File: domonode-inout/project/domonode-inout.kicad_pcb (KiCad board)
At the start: 2 copper layers, 95 x 80 mm, 54 parts, among them P1 CONN_01X03, P10 CONN_01X02, P11 CONN_01X02, P12 CONN_01X02, P13 CONN_01X02, P2 CONN_2x5, P3 CONN_01X03, P4 CONN_01X03, P5 CONN_01X03, P6 CONN_01X02, P7 CONN_01X02, P8 CONN_01X02, P9 CONN_01X02, U1 HLK-PM01, U2 PCA9555, U3 TLP620, U4 TLP620, U5 TLP620, U6 24LC02

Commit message: Updated DomoNode-Inout to 1.1.2 (improved connectors footprints)
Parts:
- added P2: Conn_01x04, AAA mie lib verificate:KF2EDGK-5.08-4, F.Cu at (123.6, 126.4)
- P1, P3, P4, P5: value CONN_01X03 -> CONN_01X02; footprint AAA mie lib verificate:AK300-3 -> AAA mie lib verificate:KF2EDGK-5.08-2
- U3, U4, U5: footprint AAA mie lib verificate:DIP-4_W7.62mm_e_SOT-4 -> Housings_DIP:DIP-4_W7.62mm
- moved P3 15.1 mm to (143.9, 126.4)
- moved P4 10.1 mm to (154.1, 126.4)
- moved P5 4.99 mm to (164.2, 126.4)
- moved P1 0.65 mm to (113.4, 126.4)
- renumbered P2 to J1
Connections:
- P3 pad 1: /RL2P -> /I1L
- P3 pad 2: /RL3P -> /I1N
- P4 pad 1: /I1L -> /I2L
- P4 pad 2: /I1N -> /I2N
- P5 pad 1: /I2N -> /I3L
- P5 pad 2: /I3L -> /I3N
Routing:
- net /I2L: track 12.5 -> 14.4 mm
- net /I2N: track 13.4 -> 15.2 mm
- net /I1N: track 12.9 -> 14.6 mm
- net Net-(R11-Pad1): track 9.80 -> 8.22 mm
- net /I3L: track 18.9 -> 20.4 mm
- net /I3N: track 16.6 -> 15.8 mm
- net /L: track 58.3 -> 57.6 mm
- net /RL2P: track 15.2 -> 14.5 mm
- net /RL3P: track 13.1 -> 12.5 mm
- net /RL4P: track 14.4 -> 13.7 mm
- net /RL1P: track 16.8 -> 16.2 mm
- net /I1L: track 11.9 -> 11.3 mm
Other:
- board text added: "DomoNode-inout 1.1.2 Design by ndk@CSSHL.org"
- board text removed: "DomoNode-inout 1.1.1 Design by ndk@CSSHL.org"

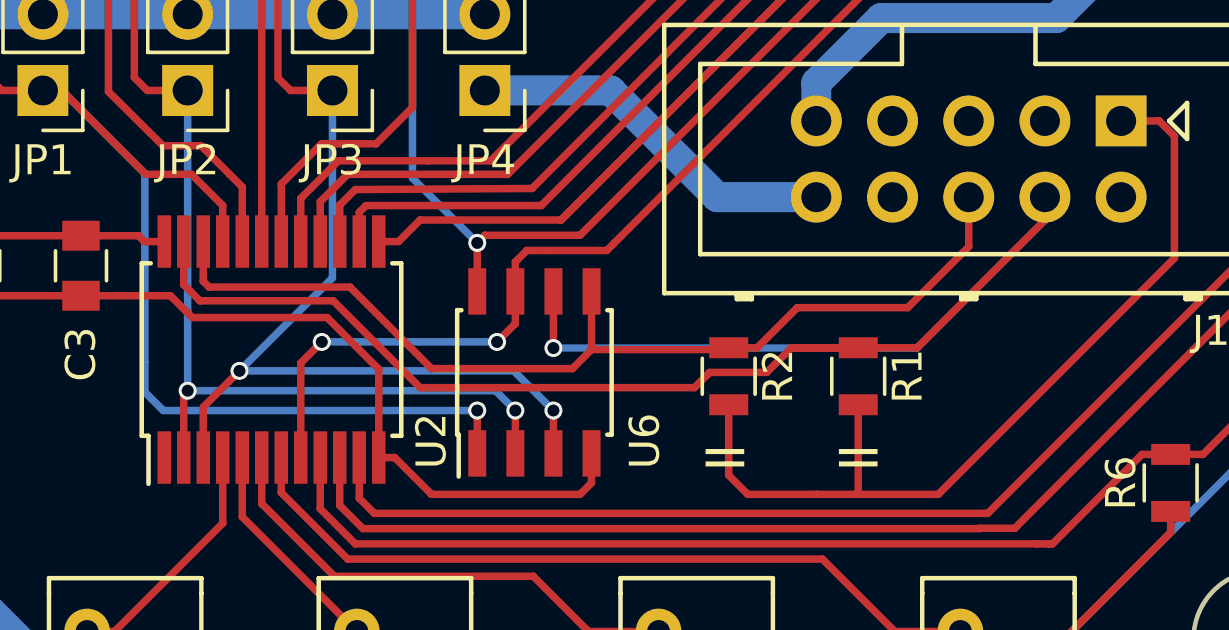
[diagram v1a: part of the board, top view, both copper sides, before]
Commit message: DomoNode-Inout: Fixed a really stupid error (swapped SCA/SCL on PCA9555); changed connector layout in schematic (from 1x10 to 2x5) for better readability
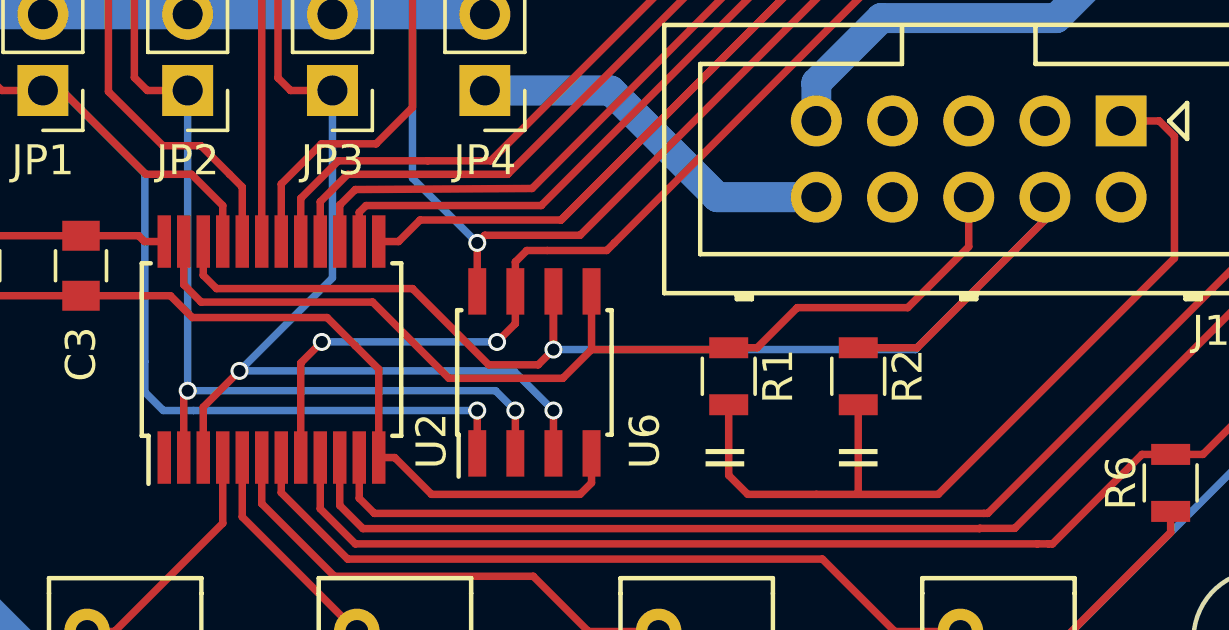
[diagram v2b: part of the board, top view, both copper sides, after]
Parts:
- moved R1 4.32 mm to (135.1, 85.5)
- moved R2 4.32 mm to (139.4, 85.5)
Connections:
- R1 pad 2: /SCL -> /SDA
- R2 pad 2: /SDA -> /SCL
- U2 pad 22: /SDA -> /SCL
- U2 pad 23: /SCL -> /SDA
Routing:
- net /SCL: track 56.9 -> 45.0 mm
- net /SDA: track 33.4 -> 34.4 mm
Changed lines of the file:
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@@
   (general
     (links 112)
-    (no_connects 1)
+    (no_connects 0)
     (area 70.765999 50.827 190.024572 139.608001)
     (thickness 1.6)
     (drawings 28)
-    (tracks 442)
+    (tracks 439)
     (zones 0)
     (modules 55)
@@
   (title_block
     (title DomoNode-InOut)
-    (date 2018-05-13)
-    (rev 1.1.2)
+    (date 2018-06-28)
+    (rev 1.1.3)
     (company CSSHL.org)
   )
@@
       (drillshape 0)
       (scaleselection 1)
-      (outputdirectory ../../../../../tmp/Domonode-inout-1.1.2/))
+      (outputdirectory ../../../../../tmp/Domonode-inout-1.1.3/))
   )
   (net 0 "")
@@
   )
   (module Resistors_SMD:R_0805 (layer F.Cu)
+    (at 135.128 85.471 90)
+    (descr "Resistor SMD 0805, reflow soldering, Vishay (see dcrcw.pdf)")
+    (tags "resistor 0805")
+    (attr smd)
+    (fp_text reference R1 (at 0 1.651 90) (layer F.SilkS)
+      (effects (font (size 1 1) (thickness 0.15)))
+    )
+    (fp_text value 10k (at 0 1.75 90) (layer F.Fab) hide
+      (effects (font (size 1 1) (thickness 0.15)))
+    )
+    (fp_text user %R (at 0 0 90) (layer F.Fab)
+      (effects (font (size 0.5 0.5) (thickness 0.075)))
+    )
+    (fp_line (start -1 0.62) (end -1 -0.62) (layer F.Fab) (width 0.1))
+    (fp_line (start 1 0.62) (end -1 0.62) (layer F.Fab) (width 0.1))
+    (fp_line (start 1 -0.62) (end 1 0.62) (layer F.Fab) (width 0.1))
+    (fp_line (start -1 -0.62) (end 1 -0.62) (layer F.Fab) (width 0.1))
+    (fp_line (start 0.6 0.88) (end -0.6 0.88) (layer F.SilkS) (width 0.12))
+    (fp_line (start -0.6 -0.88) (end 0.6 -0.88) (layer F.SilkS) (width 0.12))
+    (fp_line (start -1.55 -0.9) (end 1.55 -0.9) (layer F.CrtYd) (width 0.05))
+    (fp_line (start -1.55 -0.9) (end -1.55 0.9) (layer F.CrtYd) (width 0.05))
+    (fp_line (start 1.55 0.9) (end 1.55 -0.9) (layer F.CrtYd) (width 0.05))
+    (fp_line (start 1.55 0.9) (end -1.55 0.9) (layer F.CrtYd) (width 0.05))
+    (pad 1 smd rect (at -0.95 0 90) (size 0.7 1.3) (layers F.Cu F.Paste F.Mask)
+      (net 3 +3V3))
+    (pad 2 smd rect (at 0.95 0 90) (size 0.7 1.3) (layers F.Cu F.Paste F.Mask)
+      (net 4 /SDA))
+    (model ${KISYS3DMOD}/Resistors_SMD.3dshapes/R_0805.wrl
+      (at (xyz 0 0 0))
+      (scale (xyz 1 1 1))
+      (rotate (xyz 0 0 0))
+    )
+  )
+  (module Resistors_SMD:R_0805 (layer F.Cu)
     (at 139.446 85.471 90)
     (descr "Resistor SMD 0805, reflow soldering, Vishay (see dcrcw.pdf)")
     (tags "resistor 0805")
     (attr smd)
-    (fp_text reference R1 (at 0 1.651 90) (layer F.SilkS)
+    (fp_text reference R2 (at 0 1.651 90) (layer F.SilkS)
       (effects (font (size 1 1) (thickness 0.15)))
     )
@@
     (pad 2 smd rect (at 0.95 0 90) (size 0.7 1.3) (layers F.Cu F.Paste F.Mask)
       (net 5 /SCL))
-    (model ${KISYS3DMOD}/Resistors_SMD.3dshapes/R_0805.wrl
-      (at (xyz 0 0 0))
-      (scale (xyz 1 1 1))
-      (rotate (xyz 0 0 0))
-    )
-  )
-  (module Resistors_SMD:R_0805 (layer F.Cu)
-    (at 135.128 85.471 90)
-    (descr "Resistor SMD 0805, reflow soldering, Vishay (see dcrcw.pdf)")
-    (tags "resistor 0805")
-    (attr smd)
-    (fp_text reference R2 (at 0 1.651 90) (layer F.SilkS)
-      (effects (font (size 1 1) (thickness 0.15)))
-    )
-    (fp_text value 10k (at 0 1.75 90) (layer F.Fab) hide
-      (effects (font (size 1 1) (thickness 0.15)))
-    )
-    (fp_text user %R (at 0 0 90) (layer F.Fab)
-      (effects (font (size 0.5 0.5) (thickness 0.075)))
-    )
-    (fp_line (start -1 0.62) (end -1 -0.62) (layer F.Fab) (width 0.1))
-    (fp_line (start 1 0.62) (end -1 0.62) (layer F.Fab) (width 0.1))
-    (fp_line (start 1 -0.62) (end 1 0.62) (layer F.Fab) (width 0.1))
-    (fp_line (start -1 -0.62) (end 1 -0.62) (layer F.Fab) (width 0.1))
-    (fp_line (start 0.6 0.88) (end -0.6 0.88) (layer F.SilkS) (width 0.12))
-    (fp_line (start -0.6 -0.88) (end 0.6 -0.88) (layer F.SilkS) (width 0.12))
-    (fp_line (start -1.55 -0.9) (end 1.55 -0.9) (layer F.CrtYd) (width 0.05))
-    (fp_line (start -1.55 -0.9) (end -1.55 0.9) (layer F.CrtYd) (width 0.05))
-    (fp_line (start 1.55 0.9) (end 1.55 -0.9) (layer F.CrtYd) (width 0.05))
-    (fp_line (start 1.55 0.9) (end -1.55 0.9) (layer F.CrtYd) (width 0.05))
-    (pad 1 smd rect (at -0.95 0 90) (size 0.7 1.3) (layers F.Cu F.Paste F.Mask)
-      (net 3 +3V3))
-    (pad 2 smd rect (at 0.95 0 90) (size 0.7 1.3) (layers F.Cu F.Paste F.Mask)
-      (net 4 /SDA))
     (model ${KISYS3DMOD}/Resistors_SMD.3dshapes/R_0805.wrl
       (at (xyz 0 0 0))
@@
       (net 41 /A0))
     (pad 22 smd rect (at 3.6 -2.275 90) (size 1.75 0.45) (layers F.Cu F.Paste F.Mask)
+      (net 5 /SCL))
+    (pad 23 smd rect (at 3.6 -2.925 90) (size 1.75 0.45) (layers F.Cu F.Paste F.Mask)
       (net 4 /SDA))
-    (pad 23 smd rect (at 3.6 -2.925 90) (size 1.75 0.45) (layers F.Cu F.Paste F.Mask)
-      (net 5 /SCL))
     (pad 24 smd rect (at 3.6 -3.575 90) (size 1.75 0.45) (layers F.Cu F.Paste F.Mask)
       (net 1 +5V))
@@
   (segment (start 135.763 89.408) (end 138.049 89.408) (width 0.25) (layer F.Cu) (net 3))
   (segment (start 135.128 88.773) (end 135.763 89.408) (width 0.25) (layer F.Cu) (net 3))
+  (segment (start 117.54401 83.00001) (end 116.963 82.419) (width 0.25) (layer F.Cu) (net 4))
+  (segment (start 116.963 82.419) (end 116.963 80.982) (width 0.25) (layer F.Cu) (net 4))
+  (segment (start 130.556 84.582) (end 129.597991 85.540009) (width 0.25) (layer F.Cu) (net 4))
+  (segment (start 129.597991 85.540009) (end 125.800419 85.540009) (width 0.25) (layer F.Cu) (net 4))
+  (segment (start 125.800419 85.540009) (end 123.26042 83.00001) (width 0.25) (layer F.Cu) (net 4))
+  (segment (start 123.26042 83.00001) (end 117.54401 83.00001) (width 0.25) (layer F.Cu) (net 4))
   (segment (start 143.129 79.502) (end 143.129 81.153) (width 0.25) (layer F.Cu) (net 4) (status 10))
   (segment (start 141.097 83.185) (end 137.414 83.185) (width 0.25) (layer F.Cu) (net 4))
   (segment (start 143.129 81.153) (end 141.097 83.185) (width 0.25) (layer F.Cu) (net 4))
-  (segment (start 129.921 85.217) (end 125.222 85.217) (width 0.25) (layer F.Cu) (net 4))
-  (segment (start 117.613 80.982) (end 117.613 82.307) (width 0.25) (layer F.Cu) (net 4) (status 10))
-  (segment (start 125.222 85.217) (end 122.5042 82.4992) (width 0.25) (layer F.Cu) (net 4))
-  (segment (start 122.5042 82.4992) (end 117.8052 82.4992) (width 0.25) (layer F.Cu) (net 4))
-  (segment (start 117.8052 82.4992) (end 117.613 82.307) (width 0.25) (layer F.Cu) (net 4))
-  (segment (start 129.921 85.217) (end 130.556 84.582) (width 0.25) (layer F.Cu) (net 4))
-  (segment (start 135.128 84.521) (end 136.078 84.521) (width 0.25) (layer F.Cu) (net 4) (status 10))
   (segment (start 136.078 84.521) (end 137.414 83.185) (width 0.25) (layer F.Cu) (net 4))
   (segment (start 130.556 82.517) (end 130.556 84.582) (width 0.25) (layer F.Cu) (net 4) (status 10))
+  (segment (start 135.128 84.521) (end 136.078 84.521) (width 0.25) (layer F.Cu) (net 4) (status 10))
   (segment (start 135.1023 84.582) (end 130.556 84.582) (width 0.25) (layer F.Cu) (net 4) (status 10))
-  (segment (start 145.669 79.502) (end 145.669 80.264) (width 0.25) (layer B.Cu) (net 5) (status 30))
-  (via (at 129.286 84.5312) (size 0.6) (drill 0.4) (layers F.Cu B.Cu) (net 5))
-  (segment (start 129.286 84.5312) (end 141.4018 84.5312) (width 0.25) (layer B.Cu) (net 5))
-  (segment (start 141.4018 84.5312) (end 145.669 80.264) (width 0.25) (layer B.Cu) (net 5) (status 20))
+  (segment (start 129.286 84.582) (end 128.778 85.09) (width 0.25) (layer F.Cu) (net 5))
+  (segment (start 124.587 82.55) (end 127.127 85.09) (width 0.25) (layer F.Cu) (net 5))
+  (segment (start 118.056 82.55) (end 124.587 82.55) (width 0.25) (layer F.Cu) (net 5))
+  (segment (start 117.613 82.107) (end 117.613 80.982) (width 0.25) (layer F.Cu) (net 5))
+  (segment (start 117.613 82.107) (end 118.056 82.55) (width 0.25) (layer F.Cu) (net 5))
+  (segment (start 128.778 85.09) (end 127.127 85.09) (width 0.25) (layer F.Cu) (net 5))
+  (segment (start 145.669 79.502) (end 145.669 80.264) (width 0.25) (layer B.Cu) (net 5))
+  (segment (start 145.669 80.264) (end 141.351 84.582) (width 0.25) (layer B.Cu) (net 5))
+  (segment (start 129.286 84.582) (end 129.286 82.644) (width 0.25) (layer F.Cu) (net 5))
+  (via (at 129.286 84.582) (size 0.6) (drill 0.4) (layers F.Cu B.Cu) (net 5))
+  (segment (start 141.351 84.582) (end 129.286 84.582) (width 0.25) (layer B.Cu) (net 5))
+  (segment (start 141.412 84.521) (end 139.446 84.521) (width 0.25) (layer F.Cu) (net 5) (status 20))
   (segment (start 129.286 82.644) (end 129.286 84.5312) (width 0.25) (layer F.Cu) (net 5) (status 10))
   (segment (start 145.669 80.264) (end 141.412 84.521) (width 0.25) (layer F.Cu) (net 5) (status 10))
-  (segment (start 121.9454 82.9564) (end 124.841 85.852) (width 0.25) (layer F.Cu) (net 5))
-  (segment (start 136.398 85.344) (end 137.221 84.521) (width 0.25) (layer F.Cu) (net 5))
-  (segment (start 134.493 85.344) (end 136.398 85.344) (width 0.25) (layer F.Cu) (net 5))
-  (segment (start 133.985 85.852) (end 134.493 85.344) (width 0.25) (layer F.Cu) (net 5))
-  (segment (start 124.841 85.852) (end 133.985 85.852) (width 0.25) (layer F.Cu) (net 5))
-  (segment (start 137.221 84.521) (end 139.446 84.521) (width 0.25) (layer F.Cu) (net 5) (status 20))
-  (segment (start 116.963 80.982) (end 116.963 82.419) (width 0.25) (layer F.Cu) (net 5) (status 10))
-  (segment (start 117.5004 82.9564) (end 121.9454 82.9564) (width 0.25) (layer F.Cu) (net 5))
-  (segment (start 116.963 82.419) (end 117.5004 82.9564) (width 0.25) (layer F.Cu) (net 5))
-  (segment (start 139.446 84.521) (end 137.221 84.521) (width 0.25) (layer F.Cu) (net 5) (status 10))
-  (segment (start 141.412 84.521) (end 139.446 84.521) (width 0.25) (layer F.Cu) (net 5) (status 20))
   (segment (start 113.7412 93.98) (end 114.6556 93.98) (width 0.25) (layer F.Cu) (net 6))
   (segment (start 114.6556 93.98) (end 118.263 90.3726) (width 0.25) (layer F.Cu) (net 6))
